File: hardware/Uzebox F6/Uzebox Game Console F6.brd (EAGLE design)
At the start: 100 x 81 mm, 91 parts, among them CON1 USBSERIALSMD, IC1 MCP1700, IC2 7805T, U5 DC IN, U6 23LC1024, X1 MINI-DIN-9

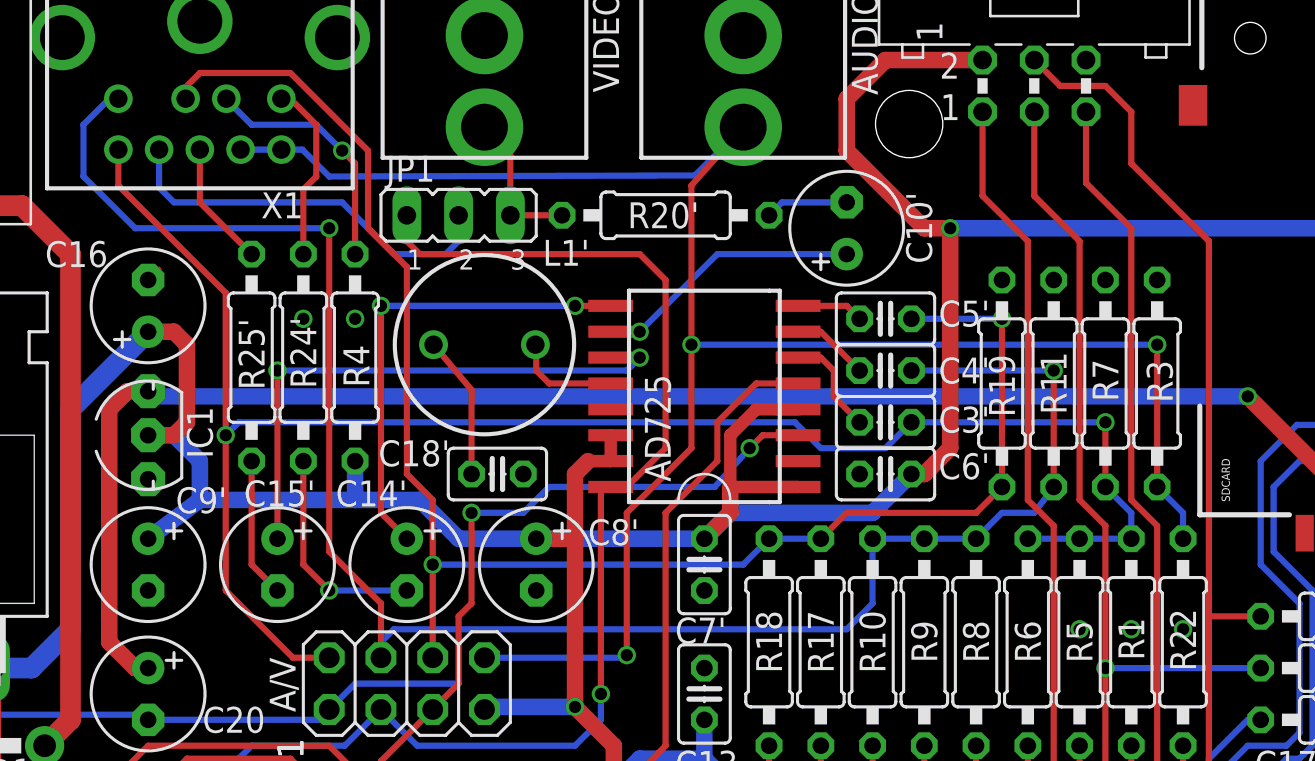
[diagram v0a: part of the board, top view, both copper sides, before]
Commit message: Update layout for better silkscreen
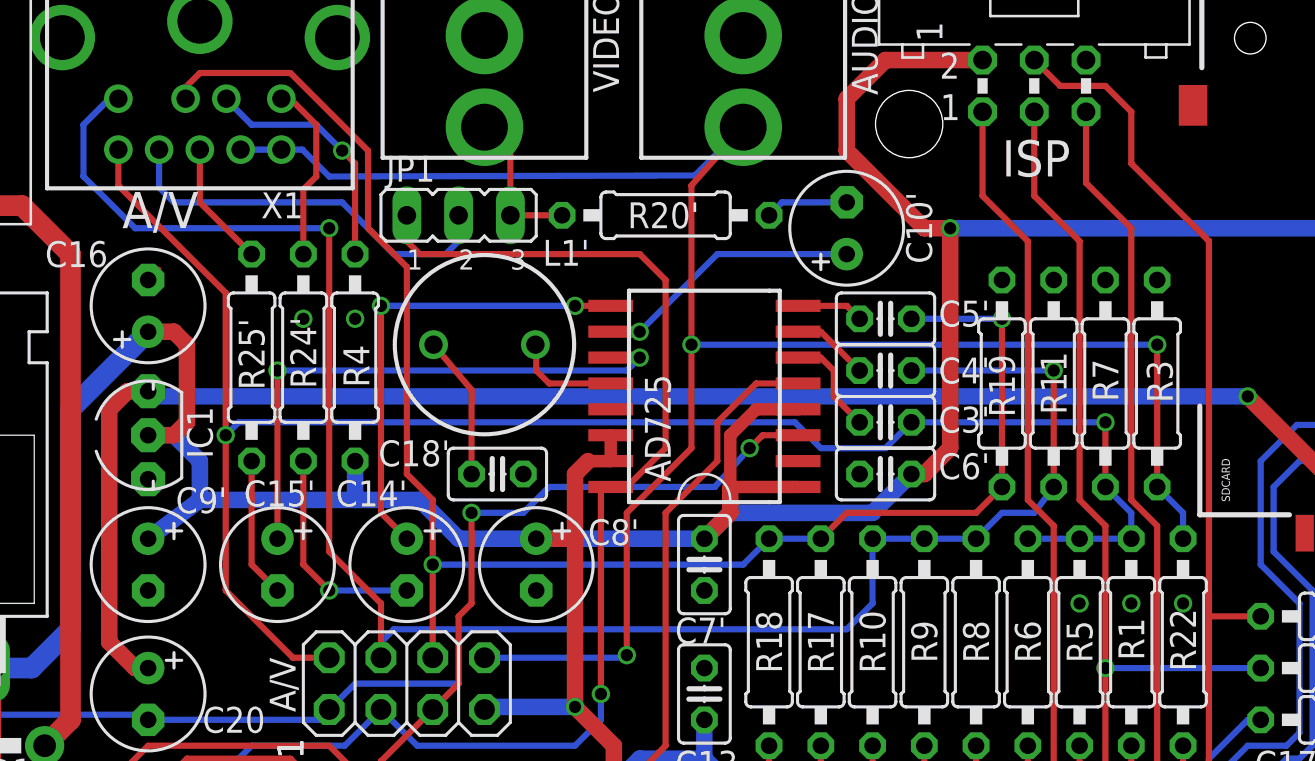
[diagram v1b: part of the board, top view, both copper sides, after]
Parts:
- X1: value MINI-DIN-9 -> A/V
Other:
- board text added: "A/V"
- board text added: "ISP"
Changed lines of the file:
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@@
 <wire x1="84.1375" y1="7.62" x2="84.7725" y2="7.62" width="0.15" layer="21"/>
 <wire x1="93.0275" y1="7.62" x2="93.6625" y2="7.62" width="0.15" layer="21"/>
+<text x="16.51" y="66.04" size="1.778" layer="21">A/V</text>
+<text x="59.69" y="68.58" size="1.778" layer="21">ISP</text>
 </plain>
 <attributes>
@@
 <attribute name="VALUE" x="75.819" y="38.989" size="1.27" layer="27" ratio="10" rot="R90"/>
 </element>
-<element name="X1" library="Thorsten_connectors" package="MINI-DIN-9" value="MINI-DIN-9" x="20.32" y="80.899" rot="R180"/>
+<element name="X1" library="Thorsten_connectors" package="MINI-DIN-9" value="A/V" x="20.32" y="80.899" rot="R180"/>
 <element name="R4" library="resistor" package="0207/10" value="180" x="27.94" y="59.69" smashed="yes" rot="R270">
 <attribute name="NAME" x="28.6385" y="58.2295" size="1.27" layer="25" ratio="10" rot="R90"/>
@@
 <contactref element="X1" pad="G2"/>
 <contactref element="X1" pad="G3"/>
-<via x="63.5" y="46.355" extent="1-16" drill="0.6"/>
-<via x="66.04" y="46.355" extent="1-16" drill="0.6"/>
-<via x="68.58" y="46.355" extent="1-16" drill="0.6"/>
+<via x="63.5" y="47.625" extent="1-16" drill="0.6"/>
+<via x="66.04" y="47.625" extent="1-16" drill="0.6"/>
+<via x="68.58" y="47.625" extent="1-16" drill="0.6"/>
 <via x="66.04" y="36.195" extent="1-16" drill="0.6"/>
 <contactref element="C19" pad="2"/>
